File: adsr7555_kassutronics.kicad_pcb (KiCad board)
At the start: 2 copper layers, 68.6 x 104.1 mm, 47 parts, among them J1 Power, J2 GateIn, J5 Atn Out, J6 Output, Q1 3904, Q2 3904, Q3 3904, Q4 3904, SW1 SW_Push, U1 7555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

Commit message: minor via moves
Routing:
- net GND: vias 8 -> 6

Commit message: created ibom and SCH.svg
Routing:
- net Net-(U2C-+): track 195.6 -> 200.7 mm
- net GND: track 267.7 -> 262.7 mm
- net -15V: vias 2 -> 4
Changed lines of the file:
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@@
+	)
+	(segment
+		(start 35.56 30.48)
+		(end 35.56 33.02)
+		(width 0.5)
+		(layer "B.Cu")
+		(net "GND")
 	)
 	(segment
@@
 	)
 	(segment
-		(start 55.88 27.94)
-		(end 35.56 27.94)
-		(width 0.5)
-		(layer "B.Cu")
-		(net "GND")
-	)
-	(segment
 		(start 71.04 76.28)
 		(end 71.12 76.2)
@@
 	)
 	(segment
-		(start 55.88 68.58)
+		(start 55.88 63.5)
 		(end 55.88 71.12)
 		(width 0.5)
@@
 	)
 	(segment
-		(start 55.88 63.5)
-		(end 55.88 66.04)
-		(width 0.5)
-		(layer "B.Cu")
-		(net "GND")
-	)
-	(segment
 		(start 81.28 86.36)
 		(end 81.28 111.76)
@@
 	)
 	(segment
+		(start 55.88 30.48)
+		(end 35.56 30.48)
+		(width 0.5)
+		(layer "B.Cu")
+		(net "GND")
+	)
+	(segment
 		(start 55.88 33.02)
 		(end 55.88 40.64)
@@
 	)
 	(segment
-		(start 55.88 66.04)
-		(end 55.88 68.58)
-		(width 0.5)
-		(layer "B.Cu")
-		(net "GND")
-	)
-	(segment
-		(start 35.56 27.94)
-		(end 35.56 33.02)
-		(width 0.5)
-		(layer "B.Cu")
-		(net "GND")
-	)
-	(segment
 		(start 76.74 85.82)
 		(end 78.74 85.82)
@@
 	(segment
 		(start 55.88 33.02)
-		(end 55.88 27.94)
+		(end 55.88 30.48)
 		(width 0.5)
 		(layer "B.Cu")
@@
 	)
 	(segment
-		(start 30.48 127)
-		(end 83.82 127)
-		(width 0.5)
-		(layer "F.Cu")
-		(net "Net-(U2C-+)")
-	)
-	(segment
 		(start 83.82 101.6)
 		(end 78.74 101.6)
@@
 	)
 	(segment
-		(start 83.82 127)
-		(end 83.82 104.14)
-		(width 0.5)
-		(layer "F.Cu")
-		(net "Net-(U2C-+)")
-	)
-	(segment
 		(start 40.64 78.74)
 		(end 40.64 91.44)
@@
 		(net "Net-(U2C-+)")
 	)
+	(via
+		(at 40.64 78.74)
+		(size 0.6)
+		(drill 0.3)
+		(layers "F.Cu" "B.Cu")
+		(net "Net-(U2C-+)")
+	)
+	(via
+		(at 78.74 101.6)
+		(size 0.6)
+		(drill 0.3)
+		(layers "F.Cu" "B.Cu")
+		(net "Net-(U2C-+)")
+	)
+	(via
+		(at 83.82 101.6)
+		(size 0.6)
+		(drill 0.3)
+		(layers "F.Cu" "B.Cu")
+		(net "Net-(U2C-+)")
+	)
+	(via
+		(at 35.56 88.9)
+		(size 0.6)
+		(drill 0.3)
+		(layers "F.Cu" "B.Cu")
+		(net "Net-(U2C-+)")
+	)
+	(via
+		(at 30.48 88.9)
+		(size 0.6)
+		(drill 0.3)
+		(layers "F.Cu" "B.Cu")
+		(net "Net-(U2C-+)")
+	)
+	(via
+		(at 40.64 91.44)
+		(size 0.6)
+		(drill 0.3)
+		(layers "F.Cu" "B.Cu")
+		(net "Net-(U2C-+)")
+	)
+	(segment
+		(start 35.56 91.44)
+		(end 35.56 88.9)
+		(width 0.5)
+		(layer "B.Cu")
+		(net "Net-(U2C-+)")
+	)
+	(segment
+		(start 86.36 101.6)
+		(end 83.82 101.6)
+		(width 0.5)
+		(layer "B.Cu")
+		(net "Net-(U2C-+)")
+	)
+	(segment
+		(start 78.74 96.52)
+		(end 78.74 101.6)
+		(width 0.5)
+		(layer "B.Cu")
+		(net "Net-(U2C-+)")
+	)
+	(segment
+		(start 83.82 83.82)
+		(end 83.82 101.6)
+		(width 0.5)
+		(layer "B.Cu")
+		(net "Net-(U2C-+)")
+	)
+	(segment
+		(start 78.74 101.6)
+		(end 63.5 101.6)
+		(width 0.5)
+		(layer "B.Cu")
+		(net "Net-(U2C-+)")
+	)
 	(segment
 		(start 30.48 88.9)
 		(end 30.48 127)
 		(width 0.5)
-		(layer "F.Cu")
-		(net "Net-(U2C-+)")
-	)
-	(via
-		(at 40.64 78.74)
-		(size 0.6)
-		(drill 0.3)
-		(layers "F.Cu" "B.Cu")
-		(net "Net-(U2C-+)")
-	)
-	(via
-		(at 78.74 101.6)
-		(size 0.6)
-		(drill 0.3)
-		(layers "F.Cu" "B.Cu")
-		(net "Net-(U2C-+)")
-	)
-	(via
-		(at 83.82 101.6)
-		(size 0.6)
-		(drill 0.3)
-		(layers "F.Cu" "B.Cu")
-		(net "Net-(U2C-+)")
-	)
-	(via
-		(at 35.56 88.9)
-		(size 0.6)
-		(drill 0.3)
-		(layers "F.Cu" "B.Cu")
-		(net "Net-(U2C-+)")
-	)
-	(via
-		(at 40.64 91.44)
-		(size 0.6)
-		(drill 0.3)
-		(layers "F.Cu" "B.Cu")
-		(net "Net-(U2C-+)")
-	)
-	(via
-		(at 83.82 104.14)
-		(size 0.6)
-		(drill 0.3)
-		(layers "F.Cu" "B.Cu")
-		(net "Net-(U2C-+)")
-	)
-	(segment
-		(start 35.56 91.44)
-		(end 35.56 88.9)
-		(width 0.5)
-		(layer "B.Cu")
-		(net "Net-(U2C-+)")
-	)
-	(segment
-		(start 78.74 96.52)
-		(end 78.74 101.6)
-		(width 0.5)
-		(layer "B.Cu")
-		(net "Net-(U2C-+)")
-	)
-	(segment
-		(start 83.82 83.82)
-		(end 83.82 101.6)
-		(width 0.5)
-		(layer "B.Cu")
-		(net "Net-(U2C-+)")
-	)
-	(segment
-		(start 78.74 101.6)
-		(end 63.5 101.6)
-		(width 0.5)
 		(layer "B.Cu")
 		(net "Net-(U2C-+)")
@@
 	)
 	(segment
-		(start 83.82 104.14)
-		(end 83.82 101.6)
+		(start 86.36 127)
+		(end 86.36 101.6)
 		(width 0.5)
 		(layer "B.Cu")
@@
 	)
 	(segment
+		(start 30.48 127)
+		(end 86.36 127)
+		(width 0.5)
+		(layer "B.Cu")
+		(net "Net-(U2C-+)")
+	)
+	(segment
 		(start 53.34 116.84)
 		(end 53.34 124.46)
@@
 	)
 	(segment
-		(start 73.66 99.06)
+		(start 66.04 35.56)
+		(end 71.12 35.56)
+		(width 0.5)
+		(layer "F.Cu")
+		(net "-15V")
+	)
+	(segment
+		(start 86.36 99.06)
+		(end 71.12 99.06)
+		(width 0.5)
+		(layer "F.Cu")
+		(net "-15V")
+	)
+	(via
+		(at 66.04 35.56)
+		(size 0.6)
+		(drill 0.3)
+		(layers "F.Cu" "B.Cu")
+		(net "-15V")
+	)
+	(via
+		(at 71.12 99.06)
+		(size 0.6)
+		(drill 0.3)
+		(layers "F.Cu" "B.Cu")
+		(net "-15V")
+	)
+	(via
+		(at 71.12 35.56)
+		(size 0.6)
+		(drill 0.3)
+		(layers "F.Cu" "B.Cu")
+		(net "-15V")
+	)
+	(via
+		(at 86.36 99.06)
+		(size 0.6)
+		(drill 0.3)
+		(layers "F.Cu" "B.Cu")
+		(net "-15V")
+	)
+	(segment
+		(start 71.12 99.06)
+		(end 63.5 99.06)
+		(width 0.5)
+		(layer "B.Cu")
+		(net "-15V")
+	)
+	(segment
+		(start 86.36 35.56)
 		(end 86.36 99.06)
 		(width 0.5)
-		(layer "F.Cu")
+		(layer "B.Cu")
 		(net "-15V")
 	)
 	(segment
-		(start 86.36 99.06)
+		(start 71.12 35.56)
 		(end 86.36 35.56)
 		(width 0.5)
-		(layer "F.Cu")
+		(layer "B.Cu")
 		(net "-15V")
 	)
 	(segment
-		(start 86.36 35.56)
+		(start 66.04 33.02)
 		(end 66.04 35.56)
-		(width 0.5)
-		(layer "F.Cu")
-		(net "-15V")
-	)
-	(via
-		(at 66.04 35.56)
-		(size 0.6)
-		(drill 0.3)
-		(layers "F.Cu" "B.Cu")
-		(net "-15V")
-	)
-	(via
-		(at 73.66 99.06)
-		(size 0.6)
-		(drill 0.3)
-		(layers "F.Cu" "B.Cu")
-		(net "-15V")
-	)
-	(segment
-		(start 66.04 35.56)
-		(end 66.04 33.02)
 		(width 0.5)
 		(layer "B.Cu")
@@
 		(width 0.5)
 		(layer "B.Cu")
-		(net "-15V")
-	)
-	(segment
-		(start 73.66 99.06)
-		(end 63.5 99.06)
-		(width 0.5)
-		(layer "B.Cu")

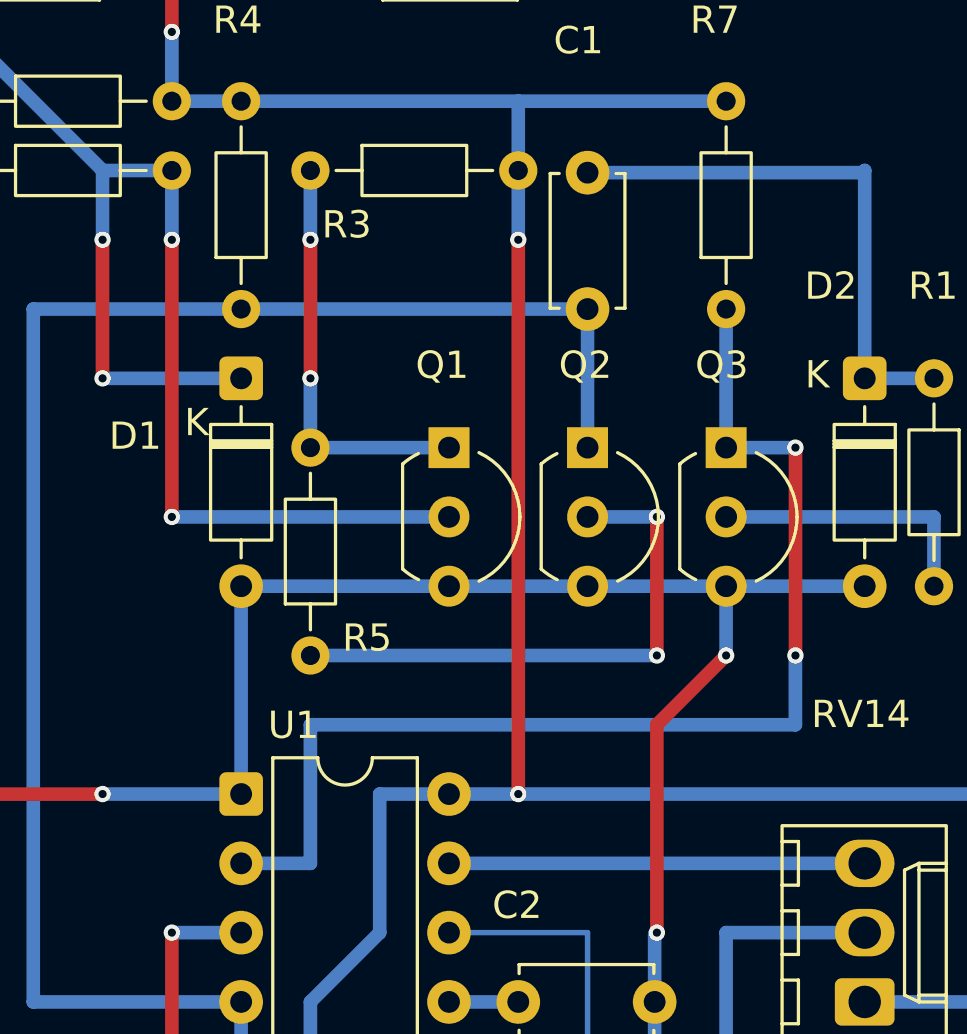
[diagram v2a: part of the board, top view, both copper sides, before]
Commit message: Wiring PCB top down. Next is U1
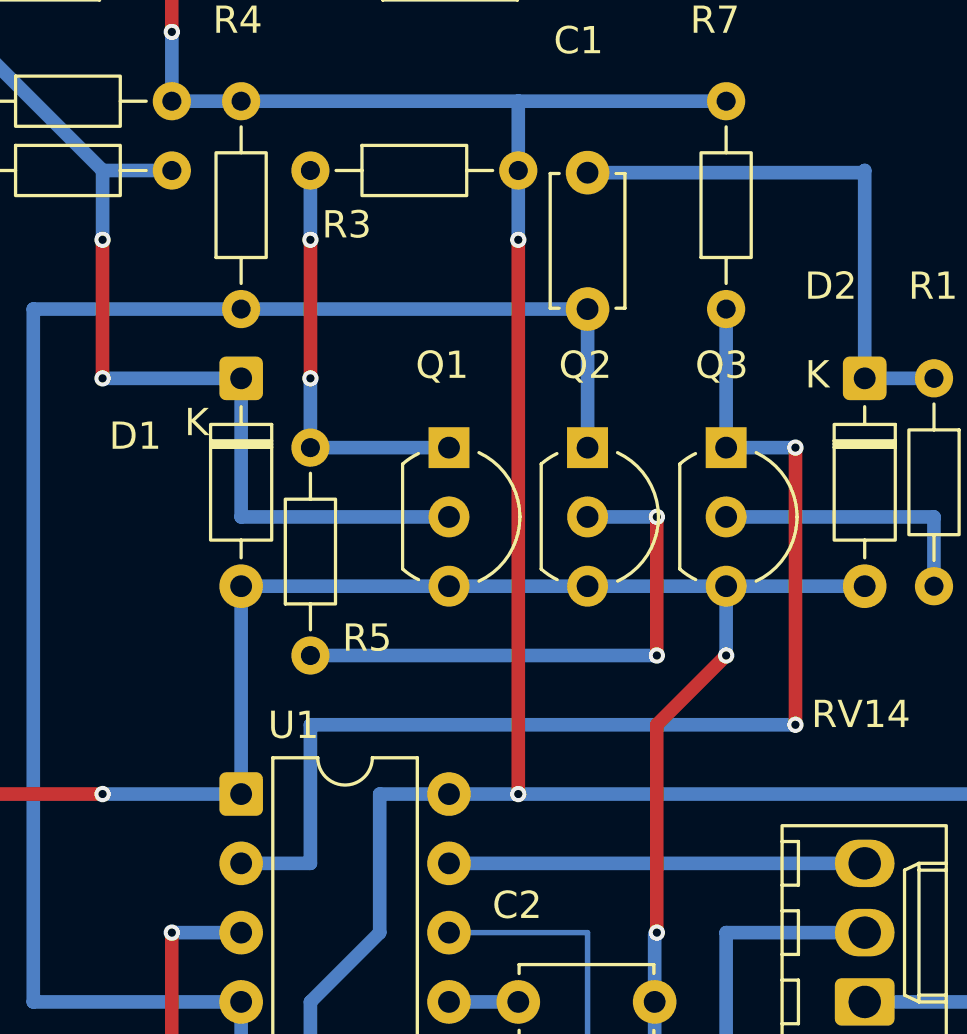
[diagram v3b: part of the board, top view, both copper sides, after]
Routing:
- net Net-(D1-K): track 50.4 -> 40.2 mm, vias 4 -> 2
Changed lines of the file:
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@@
-	)
-	(segment
-		(start 53.34 50.8)
-		(end 53.34 60.96)
-		(width 0.5)
-		(layer "F.Cu")
-		(net "Net-(D1-K)")
 	)
 	(segment
@@
 	)
 	(via
-		(at 53.34 60.96)
-		(size 0.6)
-		(drill 0.3)
-		(layers "F.Cu" "B.Cu")
-		(net "Net-(D1-K)")
-	)
-	(via
 		(at 50.8 50.8)
 		(size 0.6)
@@
 	(via
 		(at 50.8 55.88)
-		(size 0.6)
-		(drill 0.3)
-		(layers "F.Cu" "B.Cu")
-		(net "Net-(D1-K)")
-	)
-	(via
-		(at 53.34 50.8)
 		(size 0.6)
 		(drill 0.3)
@@
 	)
 	(segment
+		(start 55.88 60.96)
+		(end 63.5 60.96)
+		(width 0.5)
+		(layer "B.Cu")
+		(net "Net-(D1-K)")
+	)
+	(segment
 		(start 50.8 48.26)
 		(end 53.34 48.26)
@@
 	)
 	(segment
-		(start 53.34 48.26)
-		(end 53.34 50.8)
+		(start 55.88 60.96)
+		(end 55.88 55.88)
 		(width 0.5)
 		(layer "B.Cu")
@@
 	)
 	(segment
-		(start 53.34 60.96)
-		(end 63.5 60.96)
-		(width 0.5)
-		(layer "B.Cu")
-		(net "Net-(D1-K)")
-	)
-	(segment
 		(start 58.42 50.8)
 		(end 58.42 55.88)
@@
 	(segment
 		(start 76.2 58.42)
-		(end 76.2 66.04)
-		(width 0.5)
-		(layer "F.Cu")
-		(net "/TRIG")
-	)
-	(via
-		(at 76.2 66.04)
+		(end 76.2 68.58)
+		(width 0.5)
+		(layer "F.Cu")
+		(net "/TRIG")
+	)
+	(via
+		(at 76.2 68.58)
 		(size 0.6)
 		(drill 0.3)
@@
 	)
 	(segment
-		(start 55.88 73.66)
+		(start 58.42 73.66)
+		(end 55.88 73.66)
+		(width 0.5)
+		(layer "B.Cu")
+		(net "/TRIG")
+	)
+	(segment
+		(start 76.2 68.58)
+		(end 58.42 68.58)
+		(width 0.5)
+		(layer "B.Cu")
+		(net "/TRIG")
+	)
+	(segment
+		(start 58.42 68.58)
 		(end 58.42 73.66)
-		(width 0.5)
-		(layer "B.Cu")
-		(net "/TRIG")
-	)
-	(segment
-		(start 58.42 68.58)
-		(end 76.2 68.58)
-		(width 0.5)
-		(layer "B.Cu")
-		(net "/TRIG")
-	)
-	(segment
-		(start 76.2 68.58)
-		(end 76.2 66.04)
 		(width 0.5)
 		(layer "B.Cu")
@@
 		(width 0.5)
 		(layer "B.Cu")
-		(net "/TRIG")
-	)
-	(segment
-		(start 58.42 73.66)
-		(end 58.42 68.58)
-		(width 0.5)
-		(layer "B.Cu")
